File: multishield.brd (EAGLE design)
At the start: 57.6 x 53.7 mm, 18 parts, among them CN1 3P-2.54-90D, J2 2x16p-2.54, J4 2x6p-2.54, K2 TS-1101F, M1 ARDUINO_R3_ICSP, SW1 SK-12D01, U1 AD595AQ-DIP14, U2 ATMEGA328P_PDIP, Y1 16MHZ

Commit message: adding 100nF capacitors and minor other changes
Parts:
- added C5, C6: 100nf, Seeed-OPL-Capacitor:CERAMIC-2.54
- C1: value 100µF/16V 5X7 -> 10µF/16V
- moved Q2 1.02 mm to (33.9, 19.2)
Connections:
- net GND: now also C5.2, C6.2
- net VCC: now also C5.1, C6.1
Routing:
- net N$41: track 44.4 -> 41.9 mm
- net VCC: track 133.9 -> 136.3 mm
- net N$30: track 40.7 -> 42.5 mm
- net N$38: track 9.78 -> 11.1 mm
- net N$32: track 47.6 -> 46.4 mm
- net N$36: track 12.4 -> 11.4 mm
- net SLAVE-RESET: track 79.7 -> 79.6 mm, vias 7 -> 5

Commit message: rev 1
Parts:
- added U$4: (no value), adafruit:OSHWLOGO_BACK_0.2
- C1: value 10µF/16V -> 10µF
- moved U$1 2.17 mm to (59.0, 40.6)
- moved U$3 0.92 mm to (59.0, 14.0)
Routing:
- net N$26: track 31.3 -> 26.1 mm, vias 1 -> 0
- net N$41: track 41.9 -> 43.5 mm
- net N$32: track 46.4 -> 48.0 mm
- net N$49: track 126.2 -> 127.3 mm
- net N$46: track 37.3 -> 38.3 mm
- net N$45: track 41.3 -> 42.3 mm
- net N$50: track 83.9 -> 84.9 mm
- net N$30: track 42.5 -> 43.4 mm
- net N$25: track 24.8 -> 23.9 mm
- net N$57: track 30.4 -> 29.5 mm
- net N$35: track 38.4 -> 37.6 mm
- net N$48: track 30.4 -> 31.1 mm
- net N$47: track 34.4 -> 35.2 mm
- net N$34: track 45.4 -> 45.5 mm, vias 2 -> 3
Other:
- outline, holes or cut-outs redrawn
- board text added: "Moltoduino shield rev. 1"
- board text added: "OP"
- board text added: "PRG"
- board text removed: "Designed by Dimitris Platis for platis.solutions"
- board text removed: "Moltoduino shield rev. 0"

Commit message: latest updates
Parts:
- added J1, J3, J5, J6: 7p-2.54-90d, Seeed-OPL-Connector:H7-2.54-90D-MALE
- moved C2 1.02 mm to (49.5, 19.9)
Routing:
- net N$50: track 84.9 -> 85.8 mm
- net N$55: track 38.8 -> 39.7 mm
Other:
- board text added: "~"
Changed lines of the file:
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@@
 <layer number="20" name="Dimension" color="15" fill="1" visible="yes" active="yes"/>
 <layer number="21" name="tPlace" color="7" fill="1" visible="yes" active="yes"/>
-<layer number="22" name="bPlace" color="7" fill="1" visible="no" active="yes"/>
+<layer number="22" name="bPlace" color="7" fill="1" visible="yes" active="yes"/>
 <layer number="23" name="tOrigins" color="15" fill="1" visible="yes" active="yes"/>
 <layer number="24" name="bOrigins" color="15" fill="1" visible="yes" active="yes"/>
 <layer number="25" name="tNames" color="7" fill="1" visible="yes" active="yes"/>
-<layer number="26" name="bNames" color="7" fill="1" visible="no" active="yes"/>
+<layer number="26" name="bNames" color="7" fill="1" visible="yes" active="yes"/>
 <layer number="27" name="tValues" color="7" fill="1" visible="yes" active="yes"/>
-<layer number="28" name="bValues" color="7" fill="1" visible="no" active="yes"/>
+<layer number="28" name="bValues" color="7" fill="1" visible="yes" active="yes"/>
 <layer number="29" name="tStop" color="2" fill="3" visible="yes" active="yes"/>
 <layer number="30" name="bStop" color="5" fill="6" visible="yes" active="yes"/>
@@
 <text x="56.261" y="38.481" size="1.578" layer="21" font="vector">4</text>
 <text x="56.261" y="35.941" size="1.578" layer="21" font="vector">5</text>
-<text x="56.007" y="33.655" size="1.578" layer="21" font="vector">6</text>
+<text x="56.261" y="33.655" size="1.578" layer="21" font="vector">6</text>
 <text x="59.944" y="30.226" size="1.578" layer="21" font="vector" rot="R180">7</text>
 <text x="50.546" y="39.751" size="1.4224" layer="21" font="vector">Tx</text>
@@
 <wire x1="56.642" y1="51.054" x2="60.325" y2="51.054" width="0.4064" layer="20"/>
 <wire x1="57.277" y1="3.556" x2="60.325" y2="3.556" width="0.4064" layer="20"/>
-<wire x1="52.578" y1="31.623" x2="52.578" y2="29.845" width="0.4064" layer="21"/>
 <text x="56.769" y="9.271" size="1.3208" layer="21" font="vector" align="bottom-center">A5</text>
 <text x="56.769" y="6.731" size="1.3208" layer="21" font="vector" align="bottom-center">5V</text>
+<text x="9.398" y="32.258" size="1.578" layer="21" font="vector">~</text>
+<text x="9.398" y="29.718" size="1.578" layer="21" font="vector">~</text>
+<text x="8.509" y="27.178" size="1.578" layer="21" font="vector">~</text>
+<text x="54.991" y="40.259" size="1.578" layer="21" font="vector">~</text>
+<text x="54.991" y="35.306" size="1.578" layer="21" font="vector">~</text>
+<text x="54.991" y="32.766" size="1.578" layer="21" font="vector">~</text>
 </plain>
 <attributes>
@@
 <attribute name="VALUE" x="45.085" y="13.843" size="0.889" layer="25" ratio="11"/>
 </element>
-<element name="C2" library="Seeed-OPL-Capacitor" package="CERAMIC-2.54" value="22pf" x="48.514" y="19.939" smashed="yes">
-<attribute name="MPN" value="CS1-D5Y5V2A104ZSP" x="48.514" y="19.939" size="1.228" layer="27" display="off"/>
-<attribute name="NAME" x="46.609" y="21.209" size="0.8128" layer="25" ratio="10"/>
-<attribute name="VALUE" x="47.879" y="18.923" size="0.508" layer="25" ratio="10"/>
-<attribute name="NAME" x="47.498" y="19.685" size="0.4064" layer="33" ratio="10"/>
+<element name="C2" library="Seeed-OPL-Capacitor" package="CERAMIC-2.54" value="22pf" x="49.53" y="19.939" smashed="yes">
+<attribute name="MPN" value="CS1-D5Y5V2A104ZSP" x="49.53" y="19.939" size="1.228" layer="27" display="off"/>
+<attribute name="NAME" x="47.625" y="21.209" size="0.8128" layer="25" ratio="10"/>
+<attribute name="VALUE" x="48.895" y="18.923" size="0.508" layer="25" ratio="10"/>
+<attribute name="NAME" x="48.514" y="19.685" size="0.4064" layer="33" ratio="10"/>
 </element>
 <element name="C3" library="Seeed-OPL-Capacitor" package="CERAMIC-2.54" value="22pf" x="43.053" y="19.939" smashed="yes">
@@
 </element>
 <element name="U$4" library="adafruit" package="OSHWLOGO_BACK_0.2" value="" x="10.16" y="6.731"/>
+<element name="J1" library="Seeed-OPL-Connector" package="H7-2.54-90D-MALE" value="7p-2.54-90d" x="-20.955" y="8.255">
+<attribute name="MPN" value="P125-1107A0BR138A1" x="-20.955" y="8.255" size="1.778" layer="27" display="off"/>
+</element>
+<element name="J3" library="Seeed-OPL-Connector" package="H7-2.54-90D-MALE" value="7p-2.54-90d" x="-33.274" y="8.255">
+<attribute name="MPN" value="P125-1107A0BR138A1" x="-33.274" y="8.255" size="1.778" layer="27" display="off"/>
+</element>
+<element name="J5" library="Seeed-OPL-Connector" package="H7-2.54-90D-MALE" value="7p-2.54-90d" x="-45.593" y="8.255">
+<attribute name="MPN" value="P125-1107A0BR138A1" x="-45.593" y="8.255" size="1.778" layer="27" display="off"/>
+</element>
+<element name="J6" library="Seeed-OPL-Connector" package="H7-2.54-90D-MALE" value="7p-2.54-90d" x="-57.912" y="8.255">
+<attribute name="MPN" value="P125-1107A0BR138A1" x="-57.912" y="8.255" size="1.778" layer="27" display="off"/>
+</element>
 </elements>
 <signals>
@@
 <wire x1="47.371" y1="15.875" x2="47.371" y2="15.263" width="0.4064" layer="16"/>
 <wire x1="47.371" y1="15.263" x2="41.408" y2="9.3" width="0.4064" layer="16"/>
-<wire x1="56.007" y1="22.86" x2="50.292" y2="17.145" width="0.4064" layer="16"/>
-<wire x1="50.292" y1="17.145" x2="48.641" y2="17.145" width="0.4064" layer="16"/>
-<wire x1="56.007" y1="22.86" x2="58.9915" y2="22.86" width="0.4064" layer="16"/>
+<wire x1="50.927" y1="17.145" x2="48.641" y2="17.145" width="0.4064" layer="16"/>
+<wire x1="50.927" y1="17.145" x2="56.515" y2="22.733" width="0.4064" layer="16"/>
+<wire x1="56.515" y1="22.733" x2="58.8645" y2="22.733" width="0.4064" layer="16"/>
+<wire x1="58.8645" y1="22.733" x2="58.9915" y2="22.86" width="0.4064" layer="16"/>
 </signal>
 <signal name="N$46">
@@
 <wire x1="10.553" y1="46.355" x2="12.204" y2="48.006" width="0.4064" layer="16"/>
 <wire x1="12.204" y1="48.006" x2="52.59" y2="48.006" width="0.4064" layer="16"/>
-<wire x1="48.145" y1="26.599" x2="48.139" y2="26.593" width="0.4064" layer="16"/>
-<wire x1="51.568" y1="9.3" x2="47.371" y2="13.497" width="0.4064" layer="1"/>
+<wire x1="51.568" y1="9.3" x2="46.736" y2="14.132" width="0.4064" layer="1"/>
 <wire x1="54.968" y1="12.7" x2="51.568" y2="9.3" width="0.4064" layer="16"/>
 <contactref element="U$2" pad="7"/>
@@
 <wire x1="52.959" y1="33.276" x2="55.372" y2="35.689" width="0.4064" layer="1"/>
 <wire x1="48.139" y1="26.593" x2="48.133" y2="26.593" width="0.4064" layer="1"/>
-<wire x1="48.133" y1="26.593" x2="48.133" y2="21.463" width="0.4064" layer="1"/>
-<wire x1="48.133" y1="21.463" x2="48.387" y2="21.463" width="0.4064" layer="1"/>
-<wire x1="48.514" y1="17.653" x2="47.371" y2="16.51" width="0.4064" layer="1"/>
-<wire x1="48.387" y1="21.463" x2="48.514" y2="21.336" width="0.4064" layer="1"/>
-<wire x1="48.514" y1="21.336" x2="48.514" y2="17.653" width="0.4064" layer="1"/>
-<wire x1="47.371" y1="16.51" x2="47.371" y2="13.497" width="0.4064" layer="1"/>
 <wire x1="54.968" y1="12.7" x2="58.9915" y2="12.7" width="0.4064" layer="16"/>
 <wire x1="52.59" y1="48.006" x2="52.59" y2="47.994" width="0.4064" layer="16"/>
@@
 <via x="55.372" y="45.212" extent="1-16" drill="0.6" shape="square"/>
 <wire x1="55.372" y1="45.212" x2="55.372" y2="35.689" width="0.4064" layer="1"/>
+<wire x1="48.133" y1="26.593" x2="48.133" y2="24.384" width="0.4064" layer="1"/>
+<wire x1="48.133" y1="24.384" x2="46.736" y2="22.987" width="0.4064" layer="1"/>
+<wire x1="46.736" y1="22.987" x2="46.736" y2="14.132" width="0.4064" layer="1"/>
 <wire x1="55.372" y1="45.212" x2="54.991" y2="45.605" width="0" layer="19" extent="1-16"/>
+<wire x1="48.139" y1="26.593" x2="48.145" y2="26.599" width="0" layer="19" extent="16-16"/>
 </signal>
 <signal name="N$50">
@@
 <contactref element="U$3" pad="6"/>
 <wire x1="50.679" y1="26.593" x2="50.673" y2="26.587" width="0.4064" layer="1"/>
-<wire x1="50.673" y1="26.587" x2="50.673" y2="21.336" width="0.4064" layer="1"/>
-<wire x1="50.673" y1="21.336" x2="51.181" y2="20.828" width="0.4064" layer="1"/>
-<wire x1="51.181" y1="20.828" x2="51.181" y2="15.875" width="0.4064" layer="1"/>
-<wire x1="51.181" y1="15.875" x2="50.679" y2="15.373" width="0.4064" layer="1"/>
 <wire x1="50.679" y1="15.373" x2="50.679" y2="12.729" width="0.4064" layer="1"/>
 <wire x1="48.653" y1="32.385" x2="15.633" y2="32.385" width="0.4064" layer="1"/>
@@
 <wire x1="54.108" y1="9.3" x2="58.0045" y2="9.3" width="0.4064" layer="1"/>
 <wire x1="58.0045" y1="9.3" x2="58.9915" y2="10.16" width="0.4064" layer="1"/>
+<wire x1="50.673" y1="26.587" x2="50.673" y2="23.622" width="0.4064" layer="1"/>
+<wire x1="50.673" y1="23.622" x2="52.324" y2="21.971" width="0.4064" layer="1"/>
+<wire x1="52.324" y1="21.971" x2="52.324" y2="17.018" width="0.4064" layer="1"/>
+<wire x1="52.324" y1="17.018" x2="50.679" y2="15.373" width="0.4064" layer="1"/>
 </signal>
 <signal name="N$31">
@@
 <contactref element="Y1" pad="2"/>
 <contactref element="C2" pad="2"/>
-<wire x1="49.149" y1="15.748" x2="49.784" y2="16.383" width="0.4064" layer="1"/>
-<wire x1="49.784" y1="16.383" x2="49.784" y2="19.939" width="0.4064" layer="1"/>
-<wire x1="49.784" y1="19.939" x2="49.784" y2="24.257" width="0.4064" layer="1"/>
-<wire x1="49.784" y1="24.257" x2="49.403" y2="24.638" width="0.4064" layer="1"/>
-<wire x1="49.403" y1="24.638" x2="49.403" y2="29.083" width="0.4064" layer="1"/>
+<wire x1="49.403" y1="21.336" x2="49.403" y2="29.083" width="0.4064" layer="1"/>
 <via x="28.194" y="31.496" extent="1-16" drill="0.6" shape="square"/>
 <wire x1="28.194" y1="31.496" x2="27.819" y2="31.871" width="0.4064" layer="16"/>
@@
 <wire x1="49.403" y1="29.083" x2="46.99" y2="31.496" width="0.4064" layer="1"/>
 <wire x1="46.99" y1="31.496" x2="28.194" y2="31.496" width="0.4064" layer="1"/>
+<wire x1="49.403" y1="21.336" x2="50.8" y2="19.939" width="0.4064" layer="1"/>
+<wire x1="50.8" y1="19.939" x2="50.8" y2="17.399" width="0.4064" layer="1"/>
+<wire x1="50.8" y1="17.399" x2="49.149" y2="15.748" width="0.4064" layer="1"/>
 </signal>
 <signal name="N$57">

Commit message: 7pin angled headers instead
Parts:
- removed CN1: 3P-2.54-90D, Seeed-OPL-Connector:H3-2.54-90D-FEMALE
- removed U$1, U$2, U$3: 8p-2.54-90d, Seeed-OPL-Connector:H8-2.54-90D-FEMALE
- moved J3 92.1 mm to (58.7, 14.0)
- moved J1 86.2 mm to (58.7, 41.3)
- moved J6 64.7 mm to (5.08, 23.1), turned to 180 degrees
- moved J5 60.5 mm to (5.08, 41.3), turned to 180 degrees
- moved R3 0.90 mm to (15.4, 21.8), turned to 0 degrees
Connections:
- net GND: now also J6.5, J6.6, K2.P$1; no longer CN1.3, K2.P$2, U$3.8
- net MISO: now also J5.4; no longer U$2.5
- net MOSI: now also J5.3; no longer U$2.4
- net N$25: now also J1.1; no longer U$1.1
- net N$26: now also J1.2; no longer U$1.2
- net N$27: now also J1.3; no longer U$1.3
- net N$28: now also J1.4; no longer U$1.4
- net N$29: now also J1.5; no longer U$1.5
- net N$30: now also J1.6; no longer U$1.6
- net N$32: now also J3.1; no longer U$1.8
- net N$33: now also J6.7; no longer U$2.1
- net N$34: now also J5.1; no longer U$2.2
- net N$35: now also J5.2; no longer U$2.3
- net N$41: now also J1.7; no longer U$1.7
- net N$45: now also J3.2; no longer U$3.1
- net N$46: now also J3.3; no longer U$3.2
- net N$47: now also J3.4; no longer U$3.3
- net N$48: now also J3.5; no longer U$3.4
- net N$49: now also J3.6, J5.6; no longer U$2.7, U$3.5
- net N$50: now also J3.7, J5.7; no longer U$2.8, U$3.6
- net N$54: now also J6.3, J6.4; no longer CN1.1
- net SCK: now also J5.5; no longer U$2.6
- net SLAVE-RESET: now also K2.P$2; no longer K2.P$1
- net VCC: now also J6.1, J6.2; no longer CN1.2, U$3.7
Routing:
- net VCC: track 136.6 -> 91.6 mm, vias 2 -> 1
- net N$49: track 127.4 -> 108.8 mm
- net N$32: track 48.0 -> 57.6 mm
- net SLAVE-RESET: track 79.6 -> 87.6 mm
- net N$54: track 39.3 -> 45.5 mm, vias 1 -> 0
- net MISO: track 85.6 -> 91.4 mm, vias 3 -> 0
- net SCK: track 60.1 -> 64.7 mm
- net N$50: track 85.8 -> 90.0 mm
- net N$35: track 37.6 -> 39.8 mm, vias 2 -> 1
- net N$45: track 42.3 -> 40.2 mm
- net N$34: track 45.5 -> 47.0 mm, vias 3 -> 2
- net MOSI: track 59.4 -> 60.5 mm
- net N$46: track 38.3 -> 37.3 mm
- net N$48: track 31.1 -> 30.5 mm
- net N$27: track 25.3 -> 24.7 mm
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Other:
- outline, holes or cut-outs redrawn
- board text added: "3.3V"
- board text removed: "+3V"
- board text removed: "+5V"

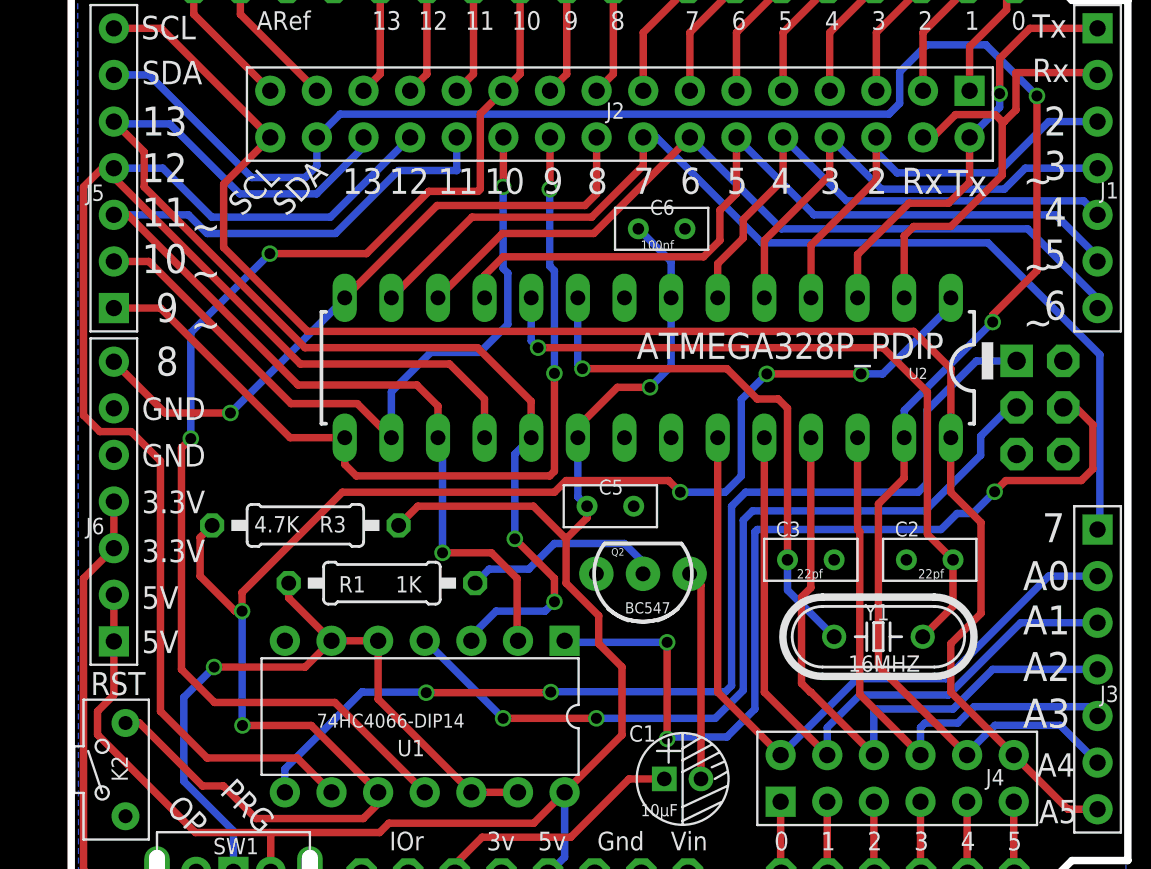
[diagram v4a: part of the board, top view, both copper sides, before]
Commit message: moved atmega328 to the left, to make more space for the isp header soldering
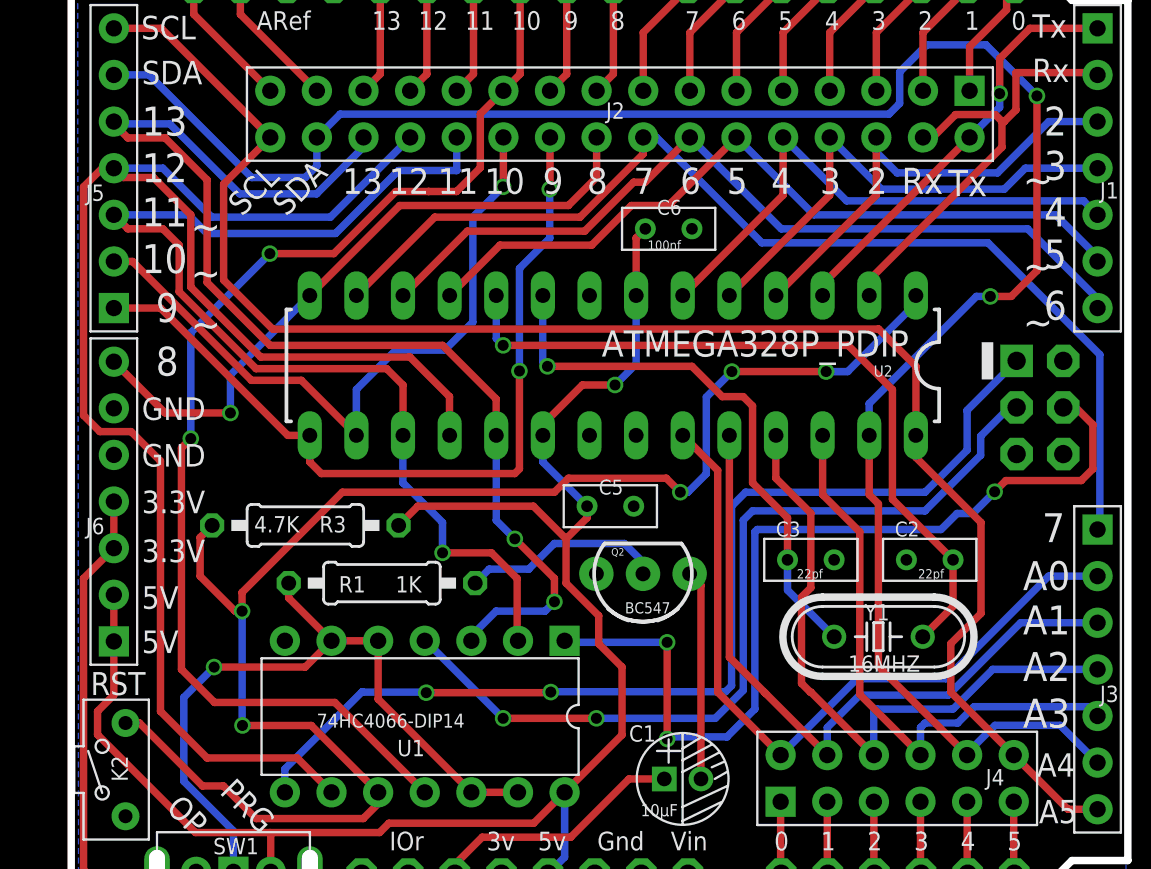
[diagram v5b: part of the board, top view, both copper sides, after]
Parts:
- moved U2 1.91 mm to (32.3, 30.5)
- moved C6 0.38 mm to (35.3, 38.0)
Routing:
- net N$41: track 43.7 -> 45.6 mm
- net SLAVE-RESET: track 87.6 -> 85.9 mm
- net N$49: track 108.8 -> 110.4 mm
- net N$30: track 43.4 -> 41.9 mm
- net N$35: track 39.8 -> 38.3 mm
- net N$34: track 47.0 -> 45.5 mm
- net N$32: track 57.6 -> 59.1 mm
- net N$53: track 58.4 -> 57.3 mm
- net MOSI: track 60.5 -> 61.5 mm
- net N$47: track 34.7 -> 35.6 mm
- net N$57: track 29.5 -> 30.5 mm
- net N$55: track 39.7 -> 40.6 mm
- net N$48: track 30.5 -> 31.5 mm
- net N$46: track 37.3 -> 38.2 mm
- net N$45: track 40.2 -> 41.1 mm
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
